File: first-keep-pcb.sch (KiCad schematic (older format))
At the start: 24 parts

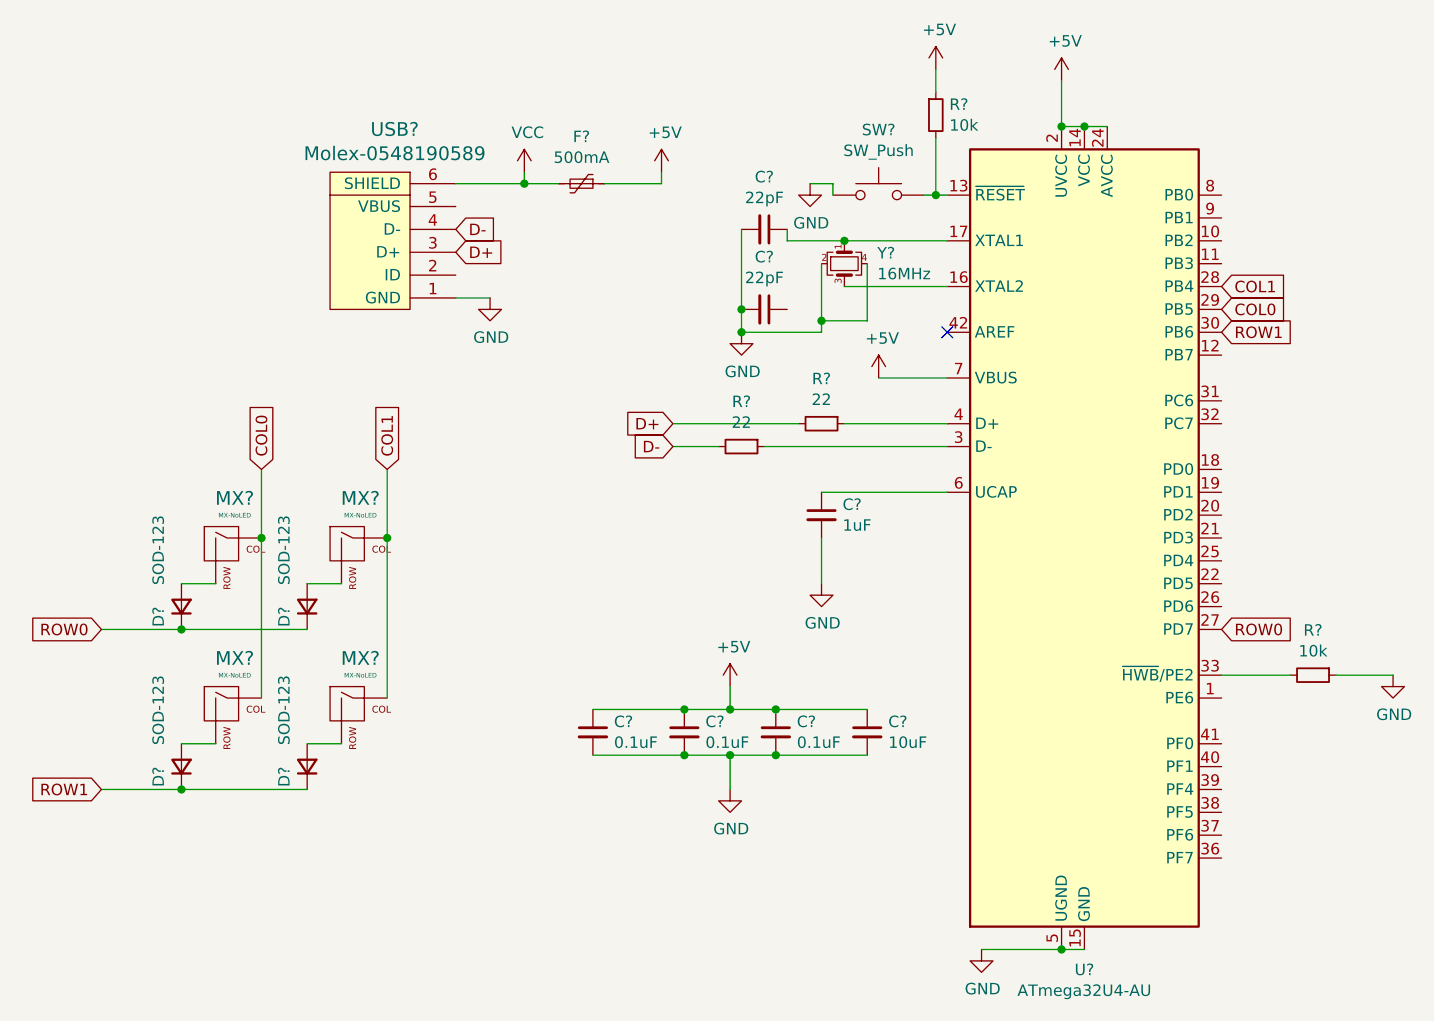
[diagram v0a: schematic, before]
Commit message: Added components to schematic
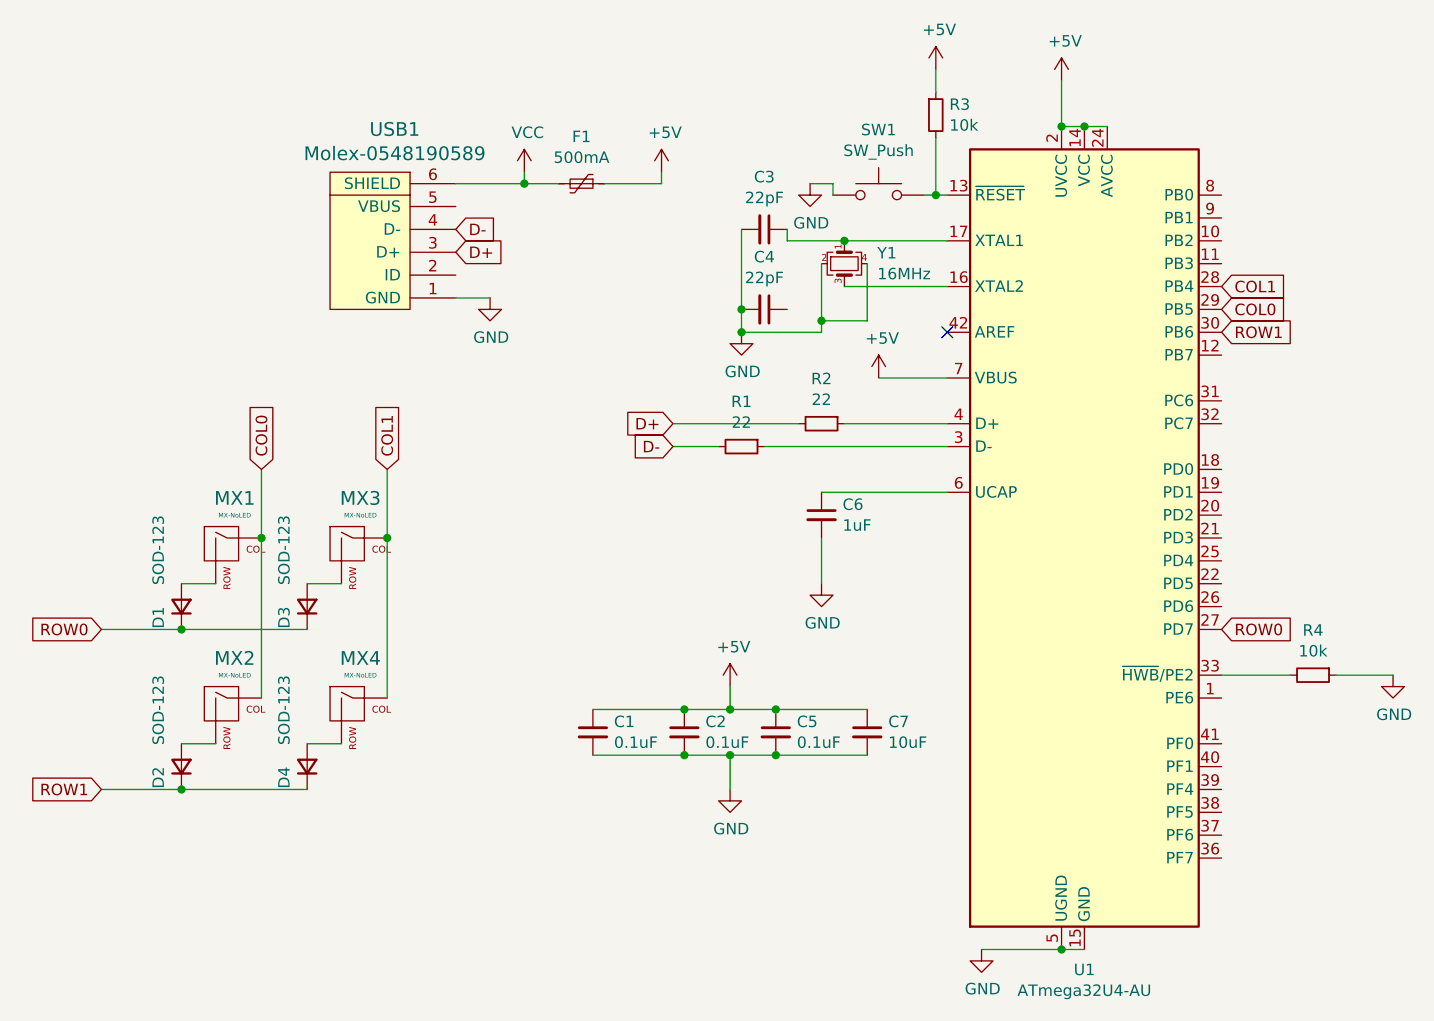
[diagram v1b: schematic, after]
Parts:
- C1, C2, C3, C4, C5, C6, C7: renamed from C?; footprint (none) -> Capacitor_SMD:C_0805_2012Metric
- D1, D2, D3, D4: renamed from D?; footprint (none) -> Diode_SMD:D_SOD-123
- F1: renamed from F?; footprint (none) -> Fuse:Fuse_1206_3216Metric
- MX1, MX2, MX3, MX4: renamed from MX?; footprint (none) -> MX_Alps_Hybrid:MX-1U-NoLED
- R1, R2, R3, R4: renamed from R?; footprint (none) -> Resistor_SMD:R_0805_2012Metric
- SW1: renamed from SW?; footprint (none) -> random-keyboard-parts:SKQG-1155865
- USB1: renamed from USB?; footprint (none) -> random-keyboard-parts:Molex-0548190589
- Y1: renamed from Y?; footprint (none) -> Crystal:Crystal_SMD_3225-4Pin_3.2x2.5mm
- gave numbers to parts that had none: 1

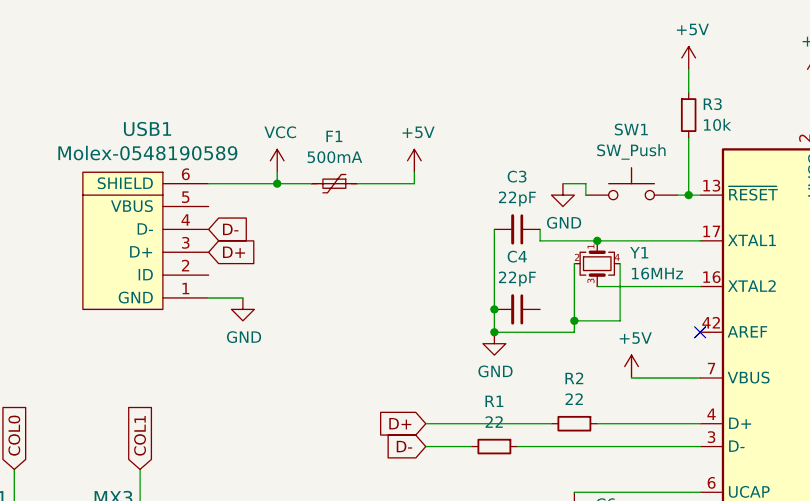
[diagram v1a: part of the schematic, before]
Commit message: Placed all pcb components
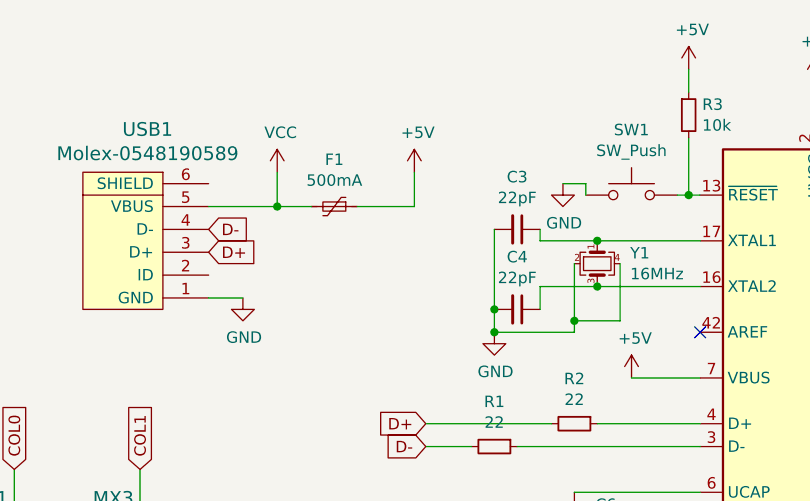
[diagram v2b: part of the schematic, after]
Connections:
- net VCC: now also USB1.5 (VBUS); no longer USB1.6 (SHIELD)
- net at U1.16 (XTAL2), Y1.3: now also C4.1
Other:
- moved on the sheet: F1
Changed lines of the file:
@@
 L Device:Polyfuse_Small F1
 U 1 1 5EEFBAE0
-P 5850 1450
-F 0 "F1" V 5645 1450 50  0000 C CNN
-F 1 "500mA" V 5736 1450 50  0000 C CNN
-F 2 "Fuse:Fuse_1206_3216Metric" H 5900 1250 50  0001 L CNN
-F 3 "~" H 5850 1450 50  0001 C CNN
-	1    5850 1450
+P 5850 1550
+F 0 "F1" V 5645 1550 50  0000 C CNN
+F 1 "500mA" V 5736 1550 50  0000 C CNN
+F 2 "Fuse:Fuse_1206_3216Metric" H 5900 1350 50  0001 L CNN
+F 3 "~" H 5850 1550 50  0001 C CNN
+	1    5850 1550
 	0    1    1    0
 $EndComp
-Wire Wire Line
-	5300 1450 5600 1450
 $Comp
 L power:VCC #PWR0111
@@
 	1    0    0    -1
 $EndComp
-Wire Wire Line
-	5600 1450 5600 1400
-Connection ~ 5600 1450
-Wire Wire Line
-	5600 1450 5750 1450
 $Comp
 L power:+5V #PWR0112
@@
 	1    0    0    -1
 $EndComp
-Wire Wire Line
-	5950 1450 6200 1450
-Wire Wire Line
-	6200 1450 6200 1400
 Text GLabel 5300 1750 2    50   Input ~ 0
 D+
@@
 Text GLabel 8650 2100 2    50   Input ~ 0
 ROW1
+Wire Wire Line
+	6750 2000 6750 1900
+Wire Wire Line
+	6750 1900 7000 1900
+Connection ~ 7000 1900
+Wire Wire Line
+	5300 1550 5600 1550
+Wire Wire Line
+	5950 1550 6200 1550
+Wire Wire Line
+	6200 1550 6200 1400
+Wire Wire Line
+	5600 1550 5600 1400
+Connection ~ 5600 1550
+Wire Wire Line
+	5600 1550 5750 1550
 $EndSCHEMATC
